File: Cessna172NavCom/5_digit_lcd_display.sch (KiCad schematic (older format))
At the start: 6 parts, among them U1 MAX7219 COM standby

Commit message: Traces for one LCD bank complete
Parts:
- LED1: value MobiFlight digit 5 -> MobiFlight digit 4
- LED2: value MobiFlight digit 4 -> MobiFlight digit 5
- LED3: value MobiFlight digit 2 -> MobiFlight digit 6
- LED4: value MobiFlight digit 1 -> MobiFlight digit 7
- LED5: value Mobiflight digit 0 -> Mobiflight digit 8
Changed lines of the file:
@@
 $Descr A4 11693 8268
 encoding utf-8
-Sheet 3 8
+Sheet 2 8
 Title ""
 Date ""
@@
 AR Path="/5F613967/5F60E2D2" Ref="U3"  Part="1"
 AR Path="/5F613974/5F60E2D2" Ref="U4"  Part="1"
-F 0 "U2" H 2500 5000 50  0000 C CNN
+F 0 "U1" H 2500 5000 50  0000 C CNN
 F 1 "MAX7219 COM standby" V 2350 4100 50  0000 C CNN
 F 2 "Package_SO:SSOP-24_3.9x8.7mm_P0.635mm" H 2700 4100 50  0001 C CNN
@@
 AR Path="/5F613967/5F60E2DE" Ref="LED11"  Part="1"
 AR Path="/5F613974/5F60E2DE" Ref="LED16"  Part="1"
-F 0 "LED6" H 4350 2900 50  0000 C CNN
-F 1 "MobiFlight digit 5" H 4350 3000 50  0000 C CNN
+F 0 "LED1" H 4350 2900 50  0000 C CNN
+F 1 "MobiFlight digit 4" H 4350 3000 50  0000 C CNN
 F 2 "Cessna 172 nav and com radio:KYX-5101AS" H 4350 2950 50  0001 C CNN
 F 3 "http://www.kingbright.com/attachments/file/psearch/000/00/00/KCSC02-105(Ver.9A).pdf" H 3850 4025 50  0001 L CNN
@@
 Text GLabel 2750 5050 3    50   Input ~ 0
 GND
-NoConn ~ 4650 3850
 Text Label 3150 3250 0    50   ~ 0
 SEG_A
@@
 Text Label 3150 4450 0    50   ~ 0
 DIG_4
-Text Label 4650 3950 0    50   ~ 0
+Text Label 4650 3850 0    50   ~ 0
 DIG_4
 Wire Wire Line
-	4650 3950 4900 3950
+	4650 3850 4900 3850
 Wire Wire Line
 	3150 4050 3450 4050
@@
 AR Path="/5F613967/5F60E317" Ref="LED12"  Part="1"
 AR Path="/5F613974/5F60E317" Ref="LED17"  Part="1"
-F 0 "LED7" H 5600 2900 50  0000 C CNN
-F 1 "MobiFlight digit 4" H 5600 3000 50  0000 C CNN
+F 0 "LED2" H 5600 2900 50  0000 C CNN
+F 1 "MobiFlight digit 5" H 5600 3000 50  0000 C CNN
 F 2 "Cessna 172 nav and com radio:KYX-5101AS" H 5600 2950 50  0001 C CNN
 F 3 "http://www.kingbright.com/attachments/file/psearch/000/00/00/KCSC02-105(Ver.9A).pdf" H 5100 4025 50  0001 L CNN
@@
 	1    0    0    -1
 $EndComp
-NoConn ~ 5900 3850
 Text Label 5300 3250 2    50   ~ 0
 SEG_A
@@
 Wire Wire Line
 	5300 3950 5000 3950
-Text Label 5900 3950 0    50   ~ 0
+Text Label 5900 3850 0    50   ~ 0
 DIG_3
 Wire Wire Line
-	5900 3950 6150 3950
+	5900 3850 6150 3850
 $Comp
 L Display_Character:KCSC02-105 LED?
@@
 AR Path="/5F613967/5F60E330" Ref="LED13"  Part="1"
 AR Path="/5F613974/5F60E330" Ref="LED18"  Part="1"
-F 0 "LED8" H 6850 2900 50  0000 C CNN
-F 1 "MobiFlight digit 2" H 6850 3000 50  0000 C CNN
+F 0 "LED3" H 6850 2900 50  0000 C CNN
+F 1 "MobiFlight digit 6" H 6850 3000 50  0000 C CNN
 F 2 "Cessna 172 nav and com radio:KYX-5101AS" H 6850 2950 50  0001 C CNN
 F 3 "http://www.kingbright.com/attachments/file/psearch/000/00/00/KCSC02-105(Ver.9A).pdf" H 6350 4025 50  0001 L CNN
@@
 	1    0    0    -1
 $EndComp
-NoConn ~ 7150 3850
 Text Label 6550 3250 2    50   ~ 0
 SEG_A
@@
 Wire Wire Line
 	6550 3950 6250 3950
-Text Label 7150 3950 0    50   ~ 0
+Text Label 7150 3850 0    50   ~ 0
 DIG_2
 Wire Wire Line
-	7150 3950 7400 3950
+	7150 3850 7400 3850
 $Comp
 L Display_Character:KCSC02-105 LED?
@@
 AR Path="/5F613967/5F60E349" Ref="LED14"  Part="1"
 AR Path="/5F613974/5F60E349" Ref="LED19"  Part="1"
-F 0 "LED9" H 8100 2900 50  0000 C CNN
-F 1 "MobiFlight digit 1" H 8100 3000 50  0000 C CNN
+F 0 "LED4" H 8100 2900 50  0000 C CNN
+F 1 "MobiFlight digit 7" H 8100 3000 50  0000 C CNN
 F 2 "Cessna 172 nav and com radio:KYX-5101AS" H 8100 2950 50  0001 C CNN
 F 3 "http://www.kingbright.com/attachments/file/psearch/000/00/00/KCSC02-105(Ver.9A).pdf" H 7600 4025 50  0001 L CNN
@@
 	1    0    0    -1
 $EndComp
-NoConn ~ 8400 3850
 Text Label 7800 3250 2    50   ~ 0
 SEG_A
@@
 Wire Wire Line
 	7800 3950 7500 3950
-Text Label 8400 3950 0    50   ~ 0
+Text Label 8400 3850 0    50   ~ 0
 DIG_1
 Wire Wire Line
-	8400 3950 8650 3950
+	8400 3850 8650 3850
 $Comp
 L Display_Character:KCSC02-105 LED?
@@
 AR Path="/5F613967/5F60E362" Ref="LED15"  Part="1"
 AR Path="/5F613974/5F60E362" Ref="LED20"  Part="1"
-F 0 "LED10" H 9350 2900 50  0000 C CNN
-F 1 "Mobiflight digit 0" H 9350 3000 50  0000 C CNN
+F 0 "LED5" H 9350 2900 50  0000 C CNN
+F 1 "Mobiflight digit 8" H 9350 3000 50  0000 C CNN
 F 2 "Cessna 172 nav and com radio:KYX-5101AS" H 9350 2950 50  0001 C CNN
 F 3 "http://www.kingbright.com/attachments/file/psearch/000/00/00/KCSC02-105(Ver.9A).pdf" H 8850 4025 50  0001 L CNN
@@
 	1    0    0    -1
 $EndComp
-NoConn ~ 9650 3850
 Text Label 9050 3250 2    50   ~ 0
 SEG_A
@@
 Wire Wire Line
 	9050 3950 8750 3950
-Text Label 9650 3950 0    50   ~ 0
+Text Label 9650 3850 0    50   ~ 0
 DIG_0
 Wire Wire Line
-	9650 3950 9900 3950
+	9650 3850 9900 3850
 Text HLabel 3150 4850 2    50   Input ~ 0
 DOUT
@@
 Text HLabel 2350 3250 0    50   Input ~ 0
 ISET
+NoConn ~ 9650 3950
+NoConn ~ 8400 3950
+NoConn ~ 7150 3950
+NoConn ~ 5900 3950
+NoConn ~ 4650 3950
 $EndSCHEMATC

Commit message: First full layout attempt, new 3D models
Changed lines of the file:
@@
 AR Path="/5F613967/5F60E2D2" Ref="U3"  Part="1"
 AR Path="/5F613974/5F60E2D2" Ref="U4"  Part="1"
-F 0 "U1" H 2500 5000 50  0000 C CNN
+F 0 "U2" H 2500 5000 50  0000 C CNN
 F 1 "MAX7219 COM standby" V 2350 4100 50  0000 C CNN
 F 2 "Package_SO:SSOP-24_3.9x8.7mm_P0.635mm" H 2700 4100 50  0001 C CNN
@@
 AR Path="/5F613967/5F60E2DE" Ref="LED11"  Part="1"
 AR Path="/5F613974/5F60E2DE" Ref="LED16"  Part="1"
-F 0 "LED1" H 4350 2900 50  0000 C CNN
+F 0 "LED6" H 4350 2900 50  0000 C CNN
 F 1 "MobiFlight digit 4" H 4350 3000 50  0000 C CNN
 F 2 "Cessna 172 nav and com radio:KYX-5101AS" H 4350 2950 50  0001 C CNN
@@
 AR Path="/5F613967/5F60E317" Ref="LED12"  Part="1"
 AR Path="/5F613974/5F60E317" Ref="LED17"  Part="1"
-F 0 "LED2" H 5600 2900 50  0000 C CNN
+F 0 "LED7" H 5600 2900 50  0000 C CNN
 F 1 "MobiFlight digit 5" H 5600 3000 50  0000 C CNN
 F 2 "Cessna 172 nav and com radio:KYX-5101AS" H 5600 2950 50  0001 C CNN
@@
 AR Path="/5F613967/5F60E330" Ref="LED13"  Part="1"
 AR Path="/5F613974/5F60E330" Ref="LED18"  Part="1"
-F 0 "LED3" H 6850 2900 50  0000 C CNN
+F 0 "LED8" H 6850 2900 50  0000 C CNN
 F 1 "MobiFlight digit 6" H 6850 3000 50  0000 C CNN
 F 2 "Cessna 172 nav and com radio:KYX-5101AS" H 6850 2950 50  0001 C CNN
@@
 AR Path="/5F613967/5F60E349" Ref="LED14"  Part="1"
 AR Path="/5F613974/5F60E349" Ref="LED19"  Part="1"
-F 0 "LED4" H 8100 2900 50  0000 C CNN
+F 0 "LED9" H 8100 2900 50  0000 C CNN
 F 1 "MobiFlight digit 7" H 8100 3000 50  0000 C CNN
 F 2 "Cessna 172 nav and com radio:KYX-5101AS" H 8100 2950 50  0001 C CNN
@@
 AR Path="/5F613967/5F60E362" Ref="LED15"  Part="1"
 AR Path="/5F613974/5F60E362" Ref="LED20"  Part="1"
-F 0 "LED5" H 9350 2900 50  0000 C CNN
+F 0 "LED10" H 9350 2900 50  0000 C CNN
 F 1 "Mobiflight digit 8" H 9350 3000 50  0000 C CNN
 F 2 "Cessna 172 nav and com radio:KYX-5101AS" H 9350 2950 50  0001 C CNN

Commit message: Re-work to use 5 digit LEDs
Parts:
- removed LED1: MobiFlight digit 4, Cessna 172 nav and com radio:KYX-5101AS, symbol Display_Character:KCSC02-105
- removed LED2: MobiFlight digit 5, Cessna 172 nav and com radio:KYX-5101AS, symbol Display_Character:KCSC02-105
- removed LED3: MobiFlight digit 6, Cessna 172 nav and com radio:KYX-5101AS, symbol Display_Character:KCSC02-105
- removed LED4: MobiFlight digit 7, Cessna 172 nav and com radio:KYX-5101AS, symbol Display_Character:KCSC02-105
- removed LED5: Mobiflight digit 8, Cessna 172 nav and com radio:KYX-5101AS, symbol Display_Character:KCSC02-105
- added U2: 3651A, Cessna 172 nav and com radio:3651A, symbol Cessna_172_nav_and_com_radio:3651A
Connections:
- wire segments 58 -> 24
- no-connect marks 8 -> 3

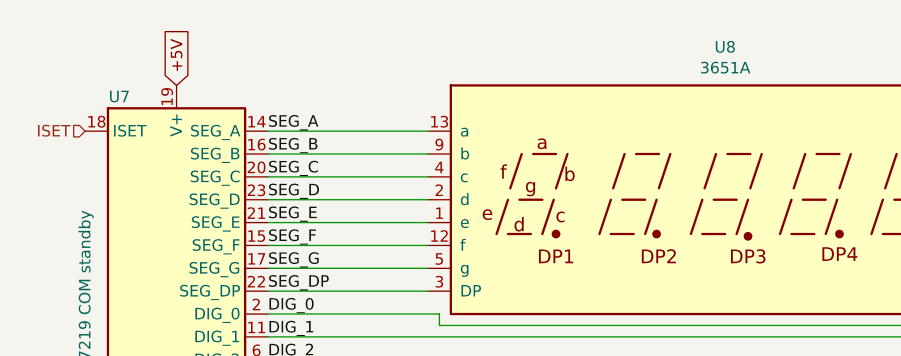
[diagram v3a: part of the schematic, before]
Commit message: Switch to USB for power, all parts on board
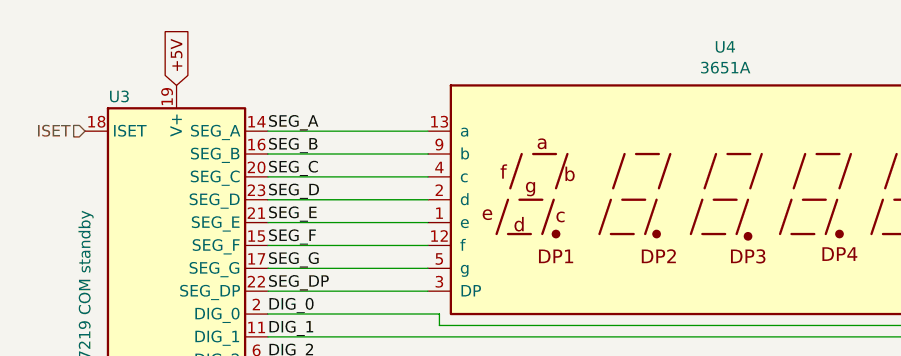
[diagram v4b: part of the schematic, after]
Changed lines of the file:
@@
 AR Path="/5F613967/5F60E2D2" Ref="U5"  Part="1"
 AR Path="/5F613974/5F60E2D2" Ref="U7"  Part="1"
-F 0 "U7" H 2500 5000 50  0000 C CNN
+F 0 "U3" H 2500 5000 50  0000 C CNN
 F 1 "MAX7219 COM standby" V 2350 4100 50  0000 C CNN
 F 2 "Package_SO:SSOP-24_3.9x8.7mm_P0.635mm" H 2700 4100 50  0001 C CNN
@@
 AR Path="/5F613974/5F5F5D43" Ref="U8"  Part="1"
 AR Path="/5F61163D/5F5F5D43" Ref="U4"  Part="1"
-F 0 "U8" H 5150 4217 50  0000 C CNN
+F 0 "U4" H 5150 4217 50  0000 C CNN
 F 1 "3651A" H 5150 4126 50  0000 C CNN
 F 2 "Cessna 172 nav and com radio:3651A" H 4950 3550 50  0001 C CNN

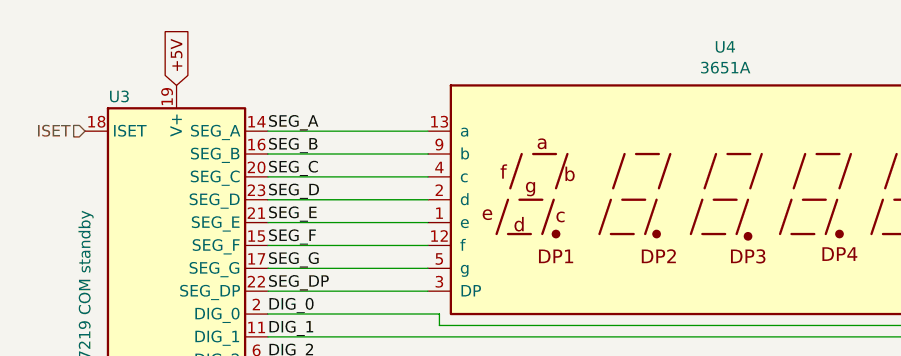
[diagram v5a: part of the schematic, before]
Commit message: Connection, footprint, and layout updates
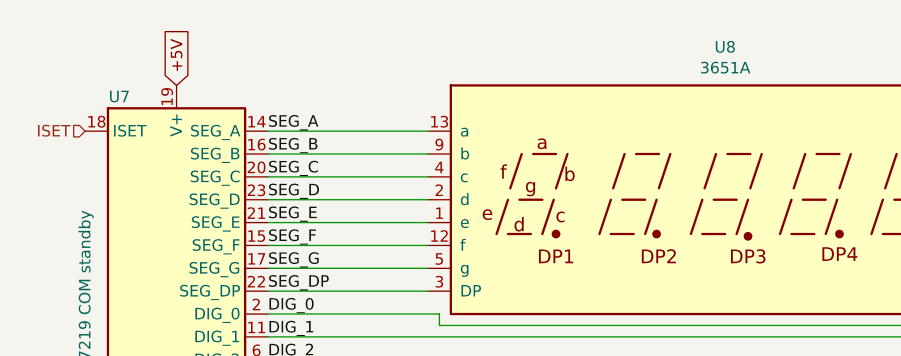
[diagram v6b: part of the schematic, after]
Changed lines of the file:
@@
 $Descr A4 11693 8268
 encoding utf-8
-Sheet 2 8
+Sheet 4 8
 Title ""
 Date ""
@@
 AR Path="/5F613967/5F60E2D2" Ref="U5"  Part="1"
 AR Path="/5F613974/5F60E2D2" Ref="U7"  Part="1"
-F 0 "U3" H 2500 5000 50  0000 C CNN
+F 0 "U7" H 2500 5000 50  0000 C CNN
 F 1 "MAX7219 COM standby" V 2350 4100 50  0000 C CNN
 F 2 "Package_SO:SSOP-24_3.9x8.7mm_P0.635mm" H 2700 4100 50  0001 C CNN
@@
 AR Path="/5F613974/5F5F5D43" Ref="U8"  Part="1"
 AR Path="/5F61163D/5F5F5D43" Ref="U4"  Part="1"
-F 0 "U4" H 5150 4217 50  0000 C CNN
+F 0 "U8" H 5150 4217 50  0000 C CNN
 F 1 "3651A" H 5150 4126 50  0000 C CNN
 F 2 "Cessna 172 nav and com radio:3651A" H 4950 3550 50  0001 C CNN

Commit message: Mostly laid out
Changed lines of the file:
@@
 $Descr A4 11693 8268
 encoding utf-8
-Sheet 4 8
+Sheet 4 15
 Title ""
 Date ""
@@
 AR Path="/5F613967/5F60E2D2" Ref="U5"  Part="1"
 AR Path="/5F613974/5F60E2D2" Ref="U7"  Part="1"
-F 0 "U7" H 2500 5000 50  0000 C CNN
+AR Path="/5F68A9CC/5F60E2D2" Ref="U9"  Part="1"
+AR Path="/5F68A9DF/5F60E2D2" Ref="U11"  Part="1"
+AR Path="/5F68A9EB/5F60E2D2" Ref="U13"  Part="1"
+AR Path="/5F68A9F8/5F60E2D2" Ref="U15"  Part="1"
+F 0 "U15" H 2500 5000 50  0000 C CNN
 F 1 "MAX7219 COM standby" V 2350 4100 50  0000 C CNN
 F 2 "Package_SO:SSOP-24_3.9x8.7mm_P0.635mm" H 2700 4100 50  0001 C CNN
@@
 AR Path="/5F613974/5F5F5D43" Ref="U8"  Part="1"
 AR Path="/5F61163D/5F5F5D43" Ref="U4"  Part="1"
-F 0 "U8" H 5150 4217 50  0000 C CNN
+AR Path="/5F68A9CC/5F5F5D43" Ref="U10"  Part="1"
+AR Path="/5F68A9DF/5F5F5D43" Ref="U12"  Part="1"
+AR Path="/5F68A9EB/5F5F5D43" Ref="U14"  Part="1"
+AR Path="/5F68A9F8/5F5F5D43" Ref="U16"  Part="1"
+F 0 "U16" H 5150 4217 50  0000 C CNN
 F 1 "3651A" H 5150 4126 50  0000 C CNN
 F 2 "Cessna 172 nav and com radio:3651A" H 4950 3550 50  0001 C CNN

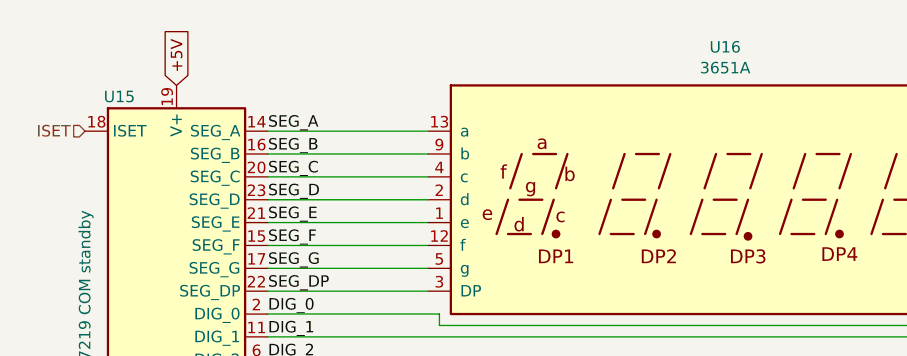
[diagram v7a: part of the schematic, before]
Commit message: Full 2up layout done
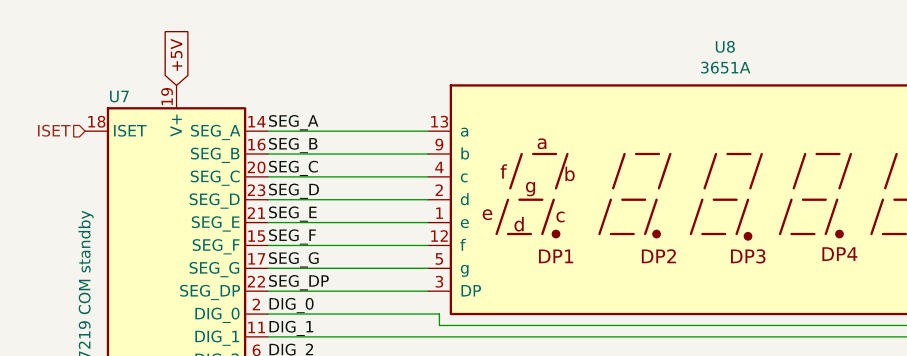
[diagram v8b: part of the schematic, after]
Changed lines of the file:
@@
 AR Path="/5F68A9EB/5F60E2D2" Ref="U13"  Part="1"
 AR Path="/5F68A9F8/5F60E2D2" Ref="U15"  Part="1"
-F 0 "U15" H 2500 5000 50  0000 C CNN
+F 0 "U7" H 2500 5000 50  0000 C CNN
 F 1 "MAX7219 COM standby" V 2350 4100 50  0000 C CNN
 F 2 "Package_SO:SSOP-24_3.9x8.7mm_P0.635mm" H 2700 4100 50  0001 C CNN
@@
 AR Path="/5F68A9EB/5F5F5D43" Ref="U14"  Part="1"
 AR Path="/5F68A9F8/5F5F5D43" Ref="U16"  Part="1"
-F 0 "U16" H 5150 4217 50  0000 C CNN
+F 0 "U8" H 5150 4217 50  0000 C CNN
 F 1 "3651A" H 5150 4126 50  0000 C CNN
 F 2 "Cessna 172 nav and com radio:3651A" H 4950 3550 50  0001 C CNN
